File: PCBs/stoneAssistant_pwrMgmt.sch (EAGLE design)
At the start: 56 parts, among them IC1 TINY2313-*S*, IC2 CNY17, IC3 CPC1976Y, IC4 CPC1976Y, T4 IRLML6402, X1 N, X2 L, X3 BTN_ON, X4 12V, X5 GND

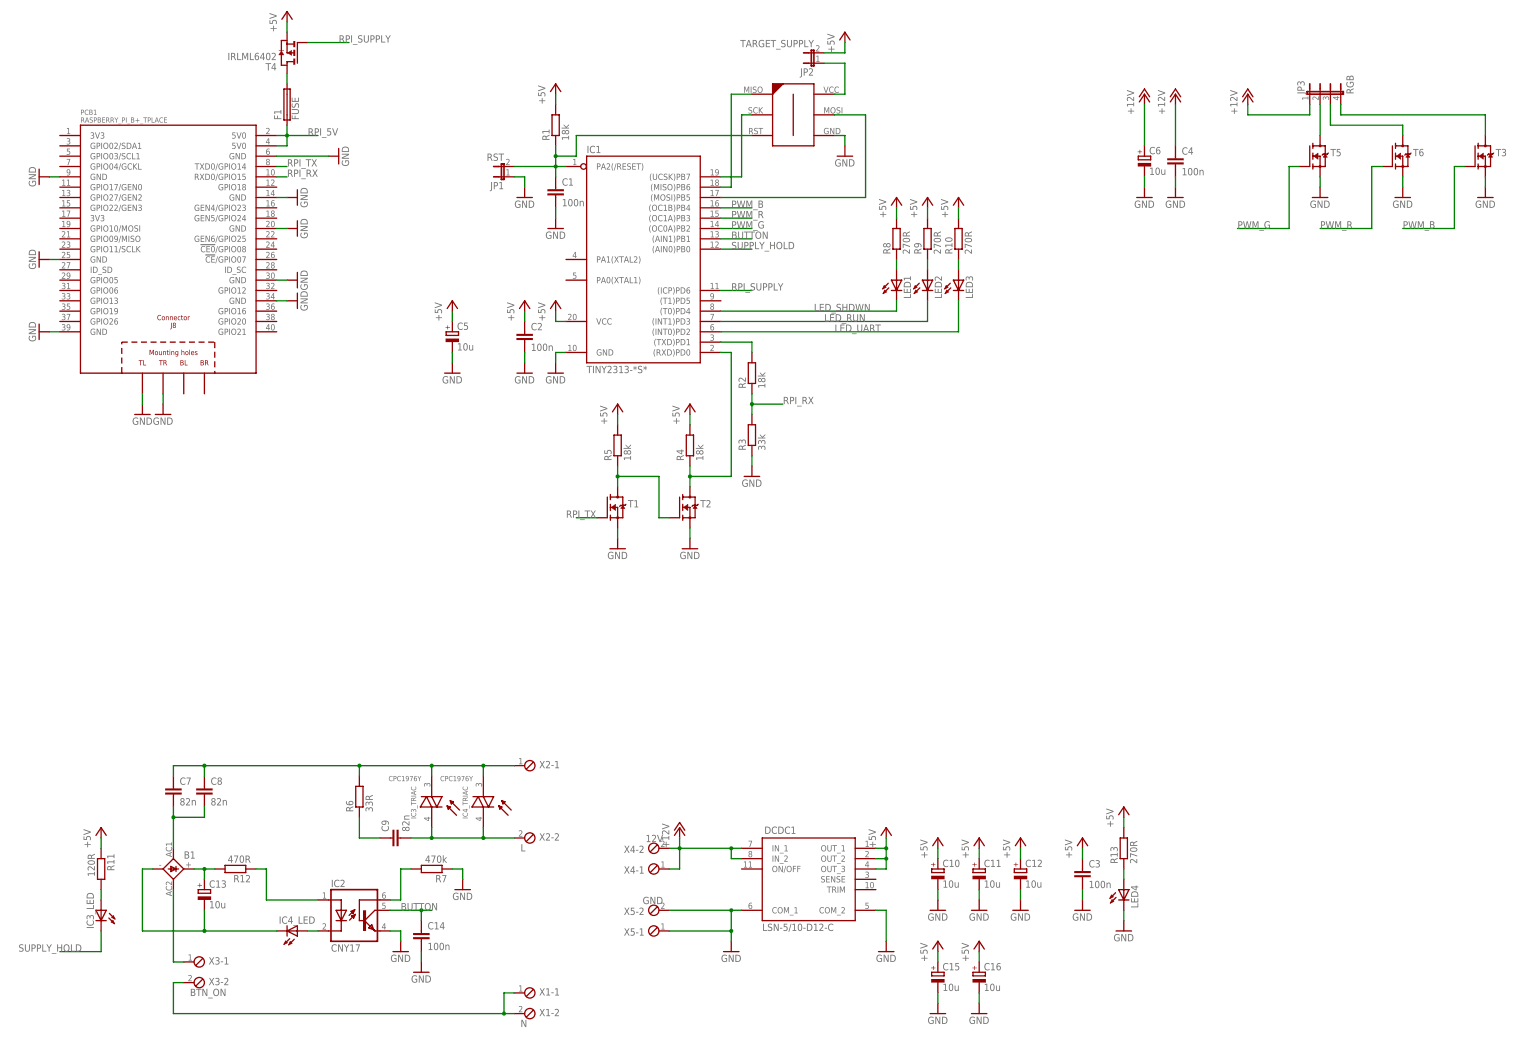
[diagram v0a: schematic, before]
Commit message: electrical: pcb redesign for better fit of components, transistor level shifter moved away from dc/dc, smd rectifier instead of tht one, cancelled out snubber, isp moved away from edge so the attiny can be programmed with the board installed on the raspberry pi
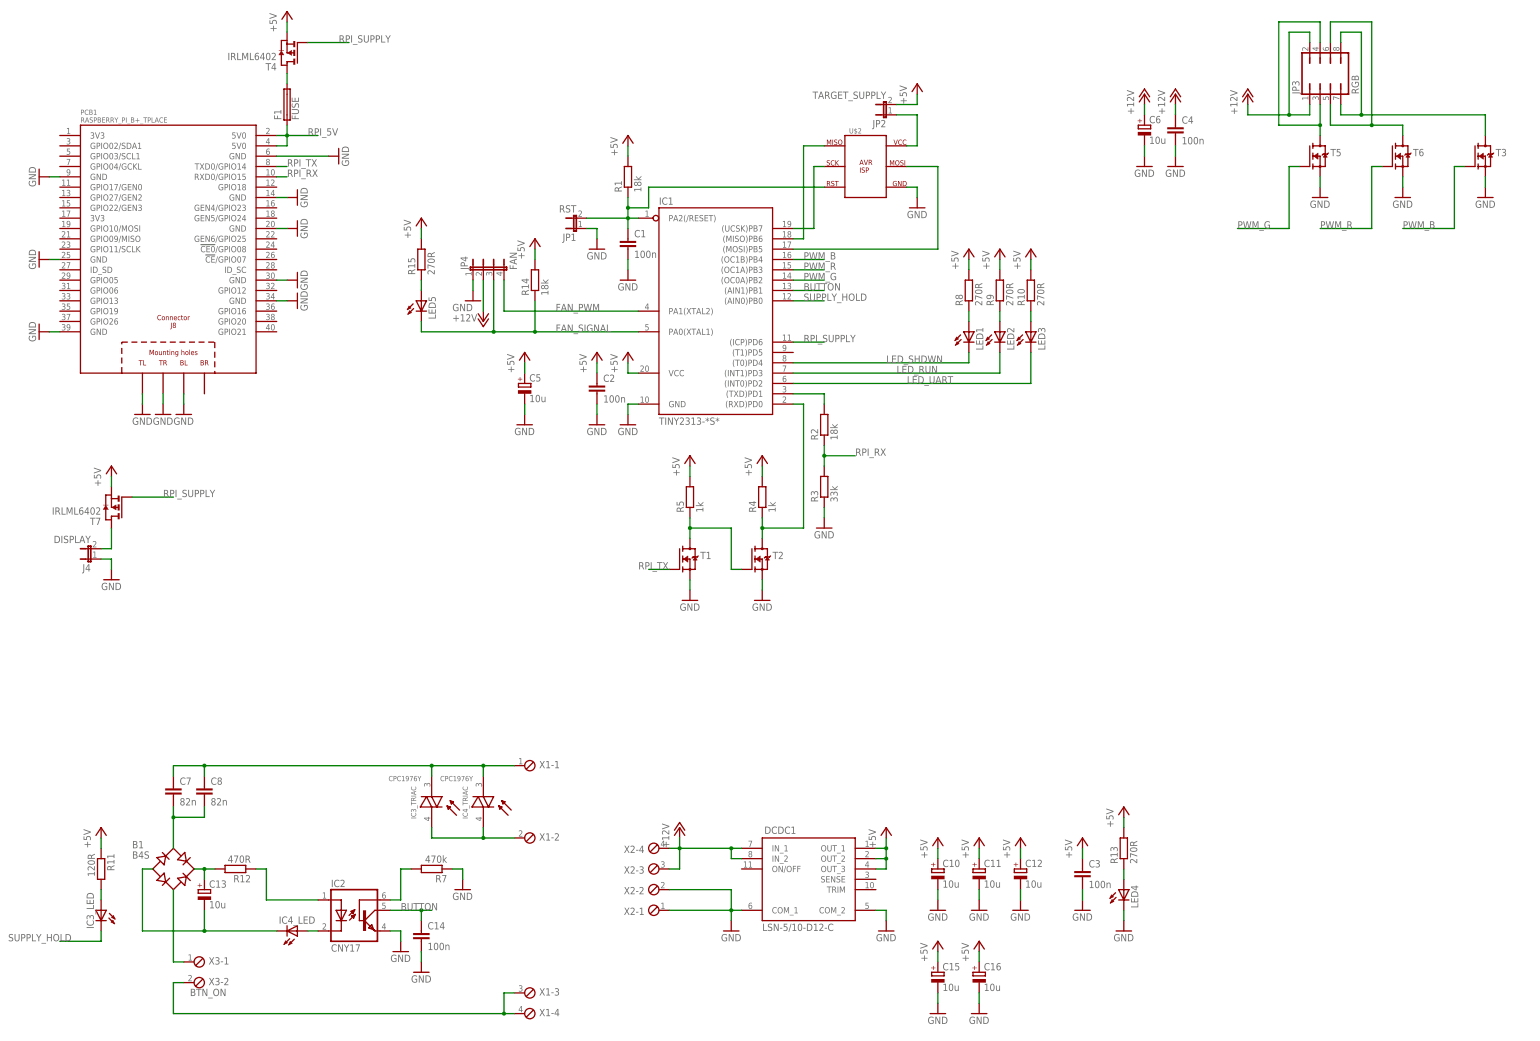
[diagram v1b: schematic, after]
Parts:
- removed C9: 82n, rcl:C-EU050-075X075
- removed R6: 33R, rcl:R-EU_M0805
- removed X4: 12V, con-phoenix-254:MPT2
- removed X5: GND, con-phoenix-254:MPT2
- added J4: DISPLAY, jumper:JP1E
- added JP4: FAN, jumper:JP4E
- added LED5: (no value), led:LEDCHIPLED_0805
- added R14: 18k, rcl:R-EU_M0805
- added R15: 270R, rcl:R-EU_M0805
- added T7: IRLML6402, IRLML6402:IRLML6402
- B1: value (none) -> B4S; device rectifier:1KAB -> rectifier:B4S
- JP3: device jumper:JP4E -> jumper:JP4Q
- R4, R5: value 18k -> 1k
- U$2: value AVR-ISP-6-EDGE -> AVR_ISPSINGLESIDED_SMD; device avr-7:AVR-ISP-6-EDGE -> stoneTronics:AVR_ISPSINGLESIDED_SMD
- X1: value N -> (none); device con-phoenix-254:MPT2 -> con-phoenix-254:MPT4
- X2: value L -> (none); device con-phoenix-254:MPT2 -> con-phoenix-254:MPT4
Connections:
- removed net N$32: C9.1, R6.1
- new net FAN_PWM: IC1.PA1(XTAL2), JP4.4
- new net FAN_SIGNAL: IC1.PA0(XTAL1), JP4.3, LED5.C, R14.1
- new net N$24: J4.2, T7.D
- new net N$25: LED5.A, R15.1
- net +12V: now also JP3.2, JP4.2, X2-3.1, X2-4.1; no longer X4-1.1, X4-2.1
- net +5V: now also R14.2, R15.2, T7.S
- net GND: now also J4.1, JP4.1, PCB1.BL, U$2.GND, X2-1.1, X2-2.1; no longer U$2.P$4, X5-1.1, X5-2.1
- net N$1: now also U$2.RST; no longer U$2.P$3
- net N$10: now also X1-2.1; no longer C9.2, X2-2.1
- net N$11: now also X1-1.1; no longer R6.2, X2-1.1
- net N$12: now also X1-3.1, X1-4.1; no longer X1-1.1, X1-2.1
- net N$21: now also JP3.3, JP3.4; no longer JP3.2
- net N$22: now also JP3.5, JP3.6; no longer JP3.3
- net N$23: now also JP3.7, JP3.8; no longer JP3.4
- net N$6: now also U$2.SCK; no longer U$2.P$2
- net N$7: now also U$2.MISO; no longer U$2.P$1
- net N$8: now also U$2.MOSI; no longer U$2.P$5
- net N$9: now also U$2.VCC; no longer U$2.P$6
- net RPI_SUPPLY: now also T7.G
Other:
- moved on the sheet: C1, C2, C4, C5, C6, IC1, JP1, JP2, LED1, LED2, LED3, R1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

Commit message: final power management pcb
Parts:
- removed JP4: FAN, jumper:JP4E
- removed LED5: (no value), led:LEDCHIPLED_0805
- removed R14: 18k, rcl:R-EU_M0805
- removed R15: 270R, rcl:R-EU_M0805
- added T8: IRLML6402, IRLML6402:IRLML6402
- added T9: IRLML2502, nxs_transistor:IRLML2502
- added X4: FAN, nxs_con-misc:PCB2_TERMINAL-BLOCK
- added X5: GND, nxs_con-misc:PCB2_TERMINAL-BLOCK
- added X6: L, nxs_con-misc:PCB2_TERMINAL-BLOCK
- T3, T5, T6: value (none) -> IRLML2502; device we-transistor:MOSFET-N-DPAK -> nxs_transistor:IRLML2502
- X1: value (none) -> BTN_ON; device con-phoenix-254:MPT4 -> nxs_con-misc:PCB2_TERMINAL-BLOCK
- X2: value (none) -> +12V; device con-phoenix-254:MPT4 -> nxs_con-misc:PCB2_TERMINAL-BLOCK
- X3: value BTN_ON -> N; device con-phoenix-254:MPT2 -> nxs_con-misc:PCB2_TERMINAL-BLOCK
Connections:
- removed net FAN_SIGNAL: IC1.PA0(XTAL1), JP4.3, LED5.C, R14.1
- new net 5V_FB: DCDC1.SENSE, T8.D
- new net N$32: PCB1.5V0@1, T8.S
- net +12V: now also X2-1.KL, X2-2.KL, X4-1.KL; no longer JP4.2, X2-3.1, X2-4.1
- net +5V: no longer R14.2, R15.2
- net FAN_PWM: now also T9.G; no longer JP4.4
- net GND: now also T9.S, X5-1.KL, X5-2.KL; no longer JP4.1, X2-1.1, X2-2.1
- net N$10: now also X6-2.KL; no longer X1-2.1
- net N$11: now also X6-1.KL; no longer X1-1.1
- net N$12: now also X1-2.KL, X3-1.KL, X3-2.KL; no longer X1-3.1, X1-4.1, X3-2.1
- net N$16: now also X1-1.KL; no longer X3-1.1
- net N$25: now also T9.D, X4-2.KL; no longer LED5.A, R15.1
- net RPI_5V: no longer PCB1.5V0@1
- net RPI_SUPPLY: now also T8.G
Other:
- note added: "FREE TO USE BY EVERYONE"
- moved on the sheet: C1, C2, C5, IC1, JP1, JP2, LED1, LED2, LED3, R1, R10, R2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

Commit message: move mechanical to thingiverse
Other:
- note added: "FOR FREE USE BY EVERYONE"
- note removed: "FREE TO USE BY EVERYONE"
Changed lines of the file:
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@@
 <sheet>
 <plain>
-<text x="322.58" y="50.8" size="5.08" layer="97">FREE TO USE
+<text x="322.58" y="50.8" size="5.08" layer="97">FOR FREE USE
 BY EVERYONE</text>
 </plain>
